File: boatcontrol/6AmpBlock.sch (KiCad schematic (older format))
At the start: 15 parts, among them U7901 ULN2803A

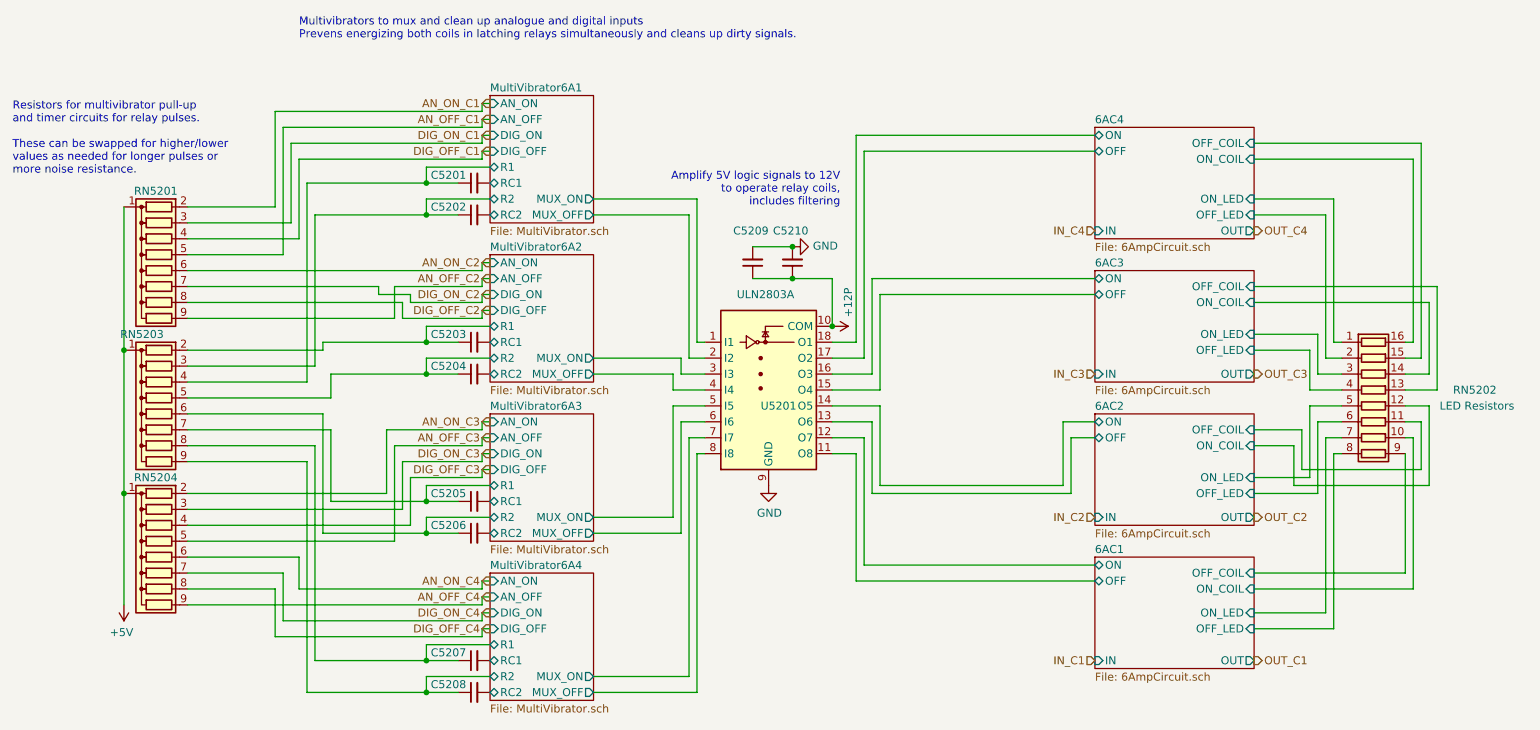
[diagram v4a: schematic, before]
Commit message: Add Node-RED flows
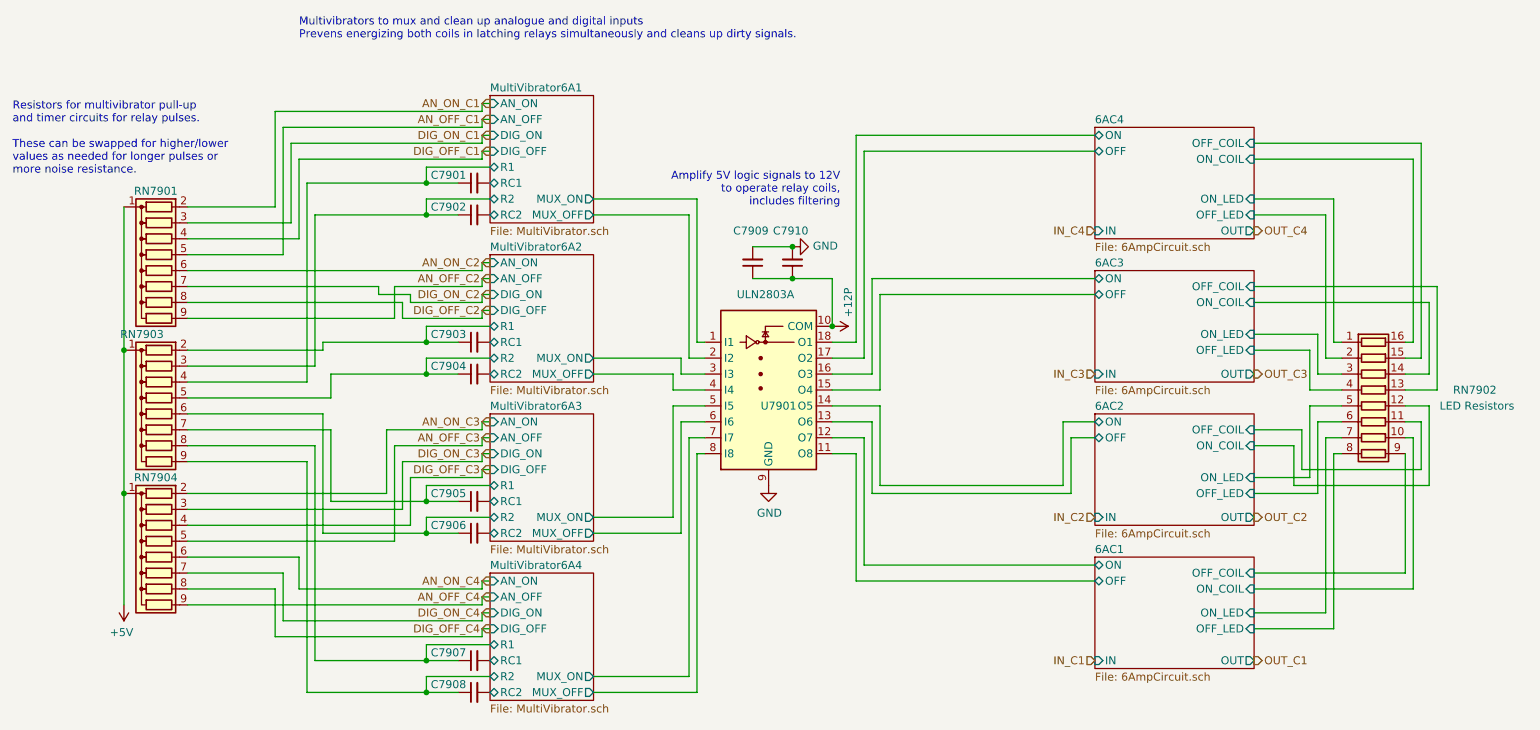
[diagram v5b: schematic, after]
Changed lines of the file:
@@
 $Descr A4 11693 8268
 encoding utf-8
-Sheet 62 97
+Sheet 89 97
 Title "Boat Control Hat"
 Date "2020-07-09"
@@
 AR Path="/D1BB8DB4/5F317CB5/60365AF1" Ref="U7901"  Part="1"
 AR Path="/D1BB8DB4/5F746103/60365AF1" Ref="U5201"  Part="1"
-F 0 "U5201" H 6250 3650 50  0000 L CNN
+F 0 "U7901" H 6250 3650 50  0000 L CNN
 F 1 "ULN2803A" H 6100 4350 50  0000 L CNN
 F 2 "Package_DIP:DIP-18_W7.62mm" H 6350 3200 50  0001 L CNN
@@
 AR Path="/D1BB8DB4/5F317CB5/60365C68" Ref="RN7902"  Part="1"
 AR Path="/D1BB8DB4/5F746103/60365C68" Ref="RN5202"  Part="1"
-F 0 "RN5202" V 10000 4550 50  0000 L CNN
+F 0 "RN7902" V 10000 4550 50  0000 L CNN
 F 1 "680Ω" V 9600 3900 50  0001 L CNN
 F 2 "BoatControl:DIP254P762X432-16P" V 10575 4050 50  0001 C CNN
@@
 AR Path="/D1BB8DB4/5F746103/62AB509B" Ref="C5201"  Part="1"
 AR Path="/D1BB8DB4/5F317CB5/62AB509B" Ref="C7901"  Part="1"
-F 0 "C5201" V 4400 2700 50  0000 L CNN
+F 0 "C7901" V 4400 2700 50  0000 L CNN
 F 1 "1µF" H 3600 2550 50  0001 L CNN
 F 2 "Capacitor_THT:C_Disc_D7.5mm_W5.0mm_P5.00mm" H 4450 2650 50  0001 C CNN
@@
 AR Path="/D1BB8DB4/5F746103/62AC1E93" Ref="C5202"  Part="1"
 AR Path="/D1BB8DB4/5F317CB5/62AC1E93" Ref="C7902"  Part="1"
-F 0 "C5202" V 4400 2900 50  0000 L CNN
+F 0 "C7902" V 4400 2900 50  0000 L CNN
 F 1 "1µF" H 3600 2750 50  0001 L CNN
 F 2 "Capacitor_THT:C_Disc_D7.5mm_W5.0mm_P5.00mm" H 4450 2850 50  0001 C CNN
@@
 AR Path="/D1BB8DB4/5F746103/62ADD9A6" Ref="C5208"  Part="1"
 AR Path="/D1BB8DB4/5F317CB5/62ADD9A6" Ref="C7908"  Part="1"
-F 0 "C5208" V 4400 5900 50  0000 L CNN
+F 0 "C7908" V 4400 5900 50  0000 L CNN
 F 1 "1µF" H 3600 5750 50  0001 L CNN
 F 2 "Capacitor_THT:C_Disc_D7.5mm_W5.0mm_P5.00mm" H 4450 5850 50  0001 C CNN
@@
 AR Path="/D1BB8DB4/5F746103/62AEACF8" Ref="C5207"  Part="1"
 AR Path="/D1BB8DB4/5F317CB5/62AEACF8" Ref="C7907"  Part="1"
-F 0 "C5207" V 4400 5700 50  0000 L CNN
+F 0 "C7907" V 4400 5700 50  0000 L CNN
 F 1 "1µF" H 3600 5550 50  0001 L CNN
 F 2 "Capacitor_THT:C_Disc_D7.5mm_W5.0mm_P5.00mm" H 4450 5650 50  0001 C CNN
@@
 AR Path="/D1BB8DB4/5F746103/62AF81A3" Ref="C5206"  Part="1"
 AR Path="/D1BB8DB4/5F317CB5/62AF81A3" Ref="C7906"  Part="1"
-F 0 "C5206" V 4400 4900 50  0000 L CNN
+F 0 "C7906" V 4400 4900 50  0000 L CNN
 F 1 "1µF" H 3600 4750 50  0001 L CNN
 F 2 "Capacitor_THT:C_Disc_D7.5mm_W5.0mm_P5.00mm" H 4450 4850 50  0001 C CNN
@@
 AR Path="/D1BB8DB4/5F746103/62B05762" Ref="C5205"  Part="1"
 AR Path="/D1BB8DB4/5F317CB5/62B05762" Ref="C7905"  Part="1"
-F 0 "C5205" V 4400 4700 50  0000 L CNN
+F 0 "C7905" V 4400 4700 50  0000 L CNN
 F 1 "1µF" H 3600 4550 50  0001 L CNN
 F 2 "Capacitor_THT:C_Disc_D7.5mm_W5.0mm_P5.00mm" H 4450 4650 50  0001 C CNN
@@
 AR Path="/D1BB8DB4/5F746103/62B3C5BA" Ref="C5203"  Part="1"
 AR Path="/D1BB8DB4/5F317CB5/62B3C5BA" Ref="C7903"  Part="1"
-F 0 "C5203" V 4400 3700 50  0000 L CNN
+F 0 "C7903" V 4400 3700 50  0000 L CNN
 F 1 "1µF" H 3600 3550 50  0001 L CNN
 F 2 "Capacitor_THT:C_Disc_D7.5mm_W5.0mm_P5.00mm" H 4450 3650 50  0001 C CNN
@@
 AR Path="/D1BB8DB4/5F746103/62B4996D" Ref="C5204"  Part="1"
 AR Path="/D1BB8DB4/5F317CB5/62B4996D" Ref="C7904"  Part="1"
-F 0 "C5204" V 4400 3900 50  0000 L CNN
+F 0 "C7904" V 4400 3900 50  0000 L CNN
 F 1 "1µF" H 3600 3750 50  0001 L CNN
 F 2 "Capacitor_THT:C_Disc_D7.5mm_W5.0mm_P5.00mm" H 4450 3850 50  0001 C CNN
@@
 AR Path="/D1BB8DB4/5F317CB5/62C7A7CE" Ref="RN7903"  Part="1"
 AR Path="/D1BB8DB4/5F746103/62C7A7CE" Ref="RN5203"  Part="1"
-F 0 "RN5203" V 1950 4050 50  0000 L CNN
+F 0 "RN7903" V 1950 4050 50  0000 L CNN
 F 1 "10MΩ" H 2100 3700 50  0001 L CNN
 F 2 "Resistor_THT:R_Array_SIP9" V 2925 4100 50  0001 C CNN
@@
 AR Path="/D1BB8DB4/5F317CB5/62F1D24C" Ref="RN7904"  Part="1"
 AR Path="/D1BB8DB4/5F746103/62F1D24C" Ref="RN5204"  Part="1"
-F 0 "RN5204" V 1950 5000 50  0000 C CNN
+F 0 "RN7904" V 1950 5000 50  0000 C CNN
 F 1 "100KΩ" V 2250 4700 50  0001 C CNN
 F 2 "Resistor_THT:R_Array_SIP9" H 3200 5100 50  0001 L CNN
@@
 AR Path="/D1BB8DB4/5F317CB5/62F2A731" Ref="RN7901"  Part="1"
 AR Path="/D1BB8DB4/5F746103/62F2A731" Ref="RN5201"  Part="1"
-F 0 "RN5201" V 1950 3200 50  0000 C CNN
+F 0 "RN7901" V 1950 3200 50  0000 C CNN
 F 1 "100KΩ" V 2250 2900 50  0001 C CNN
 F 2 "Resistor_THT:R_Array_SIP9" H 3200 3300 50  0001 L CNN
@@
 AR Path="/D1BB8DB4/5F317CB5/624D8B2F" Ref="C7909"  Part="1"
 AR Path="/D1BB8DB4/5F746103/624D8B2F" Ref="C5209"  Part="1"
-F 0 "C5209" H 6100 2950 50  0000 L CNN
+F 0 "C7909" H 6100 2950 50  0000 L CNN
 F 1 "10uF" H 6291 3105 50  0001 L CNN
 F 2 "Capacitor_THT:C_Disc_D7.5mm_W5.0mm_P5.00mm" H 6200 3150 50  0001 C CNN
@@
 AR Path="/D1BB8DB4/5F317CB5/624D8B37" Ref="C7910"  Part="1"
 AR Path="/D1BB8DB4/5F746103/624D8B37" Ref="C5210"  Part="1"
-F 0 "C5210" H 6350 2950 50  0000 L CNN
+F 0 "C7910" H 6350 2950 50  0000 L CNN
 F 1 "0.1uF" H 6541 3105 50  0001 L CNN
 F 2 "Capacitor_THT:C_Disc_D7.5mm_W5.0mm_P5.00mm" H 6450 3150 50  0001 C CNN

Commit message: Fix SB footprint and symbol
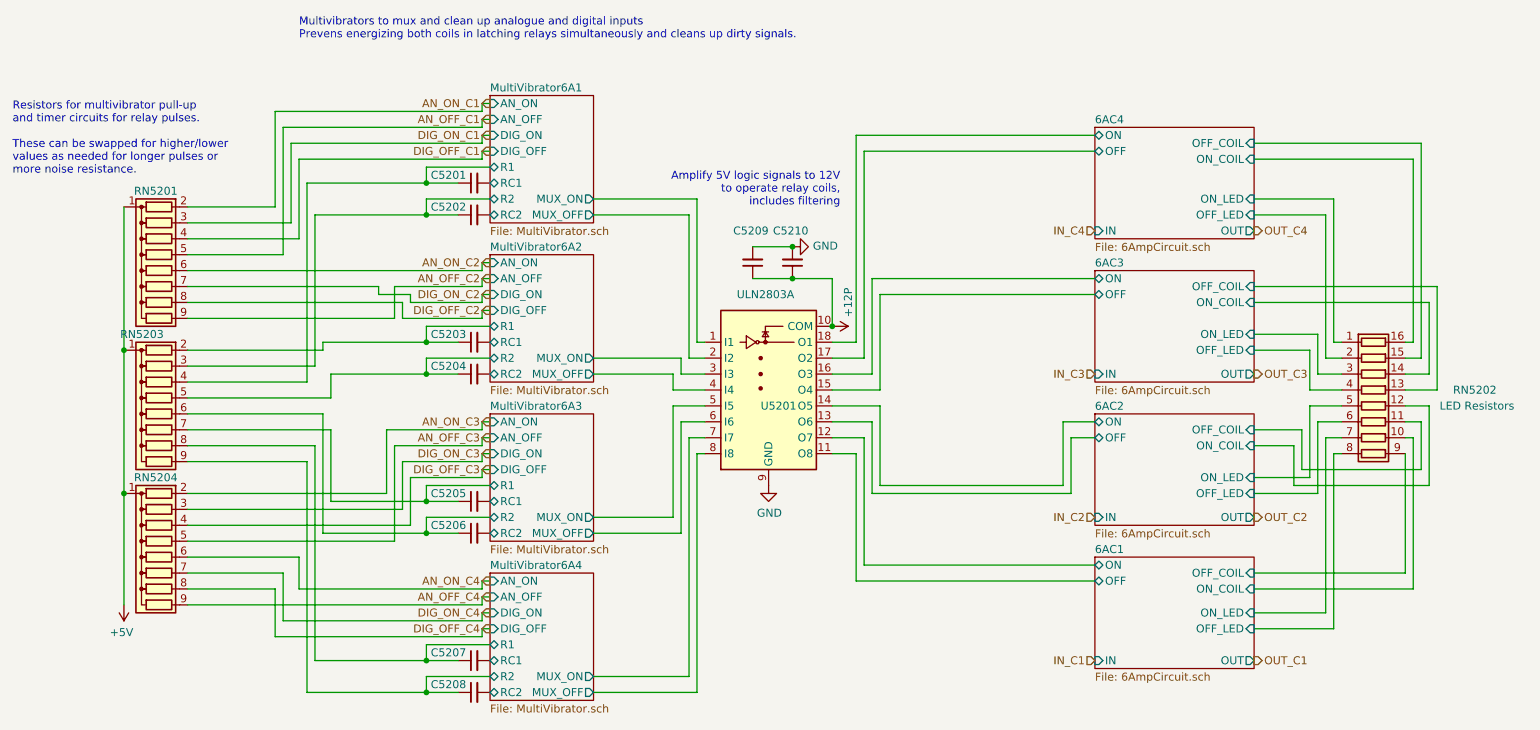
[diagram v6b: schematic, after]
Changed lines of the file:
@@
 $Descr A4 11693 8268
 encoding utf-8
-Sheet 89 97
+Sheet 51 97
 Title "Boat Control Hat"
 Date "2020-07-09"
@@
 AR Path="/D1BB8DB4/5F317CB5/60365AF1" Ref="U7901"  Part="1"
 AR Path="/D1BB8DB4/5F746103/60365AF1" Ref="U5201"  Part="1"
-F 0 "U7901" H 6250 3650 50  0000 L CNN
+F 0 "U5201" H 6250 3650 50  0000 L CNN
 F 1 "ULN2803A" H 6100 4350 50  0000 L CNN
 F 2 "Package_DIP:DIP-18_W7.62mm" H 6350 3200 50  0001 L CNN
@@
 AR Path="/D1BB8DB4/5F317CB5/60365C68" Ref="RN7902"  Part="1"
 AR Path="/D1BB8DB4/5F746103/60365C68" Ref="RN5202"  Part="1"
-F 0 "RN7902" V 10000 4550 50  0000 L CNN
+F 0 "RN5202" V 10000 4550 50  0000 L CNN
 F 1 "680Ω" V 9600 3900 50  0001 L CNN
 F 2 "BoatControl:DIP254P762X432-16P" V 10575 4050 50  0001 C CNN
@@
 AR Path="/D1BB8DB4/5F746103/62AB509B" Ref="C5201"  Part="1"
 AR Path="/D1BB8DB4/5F317CB5/62AB509B" Ref="C7901"  Part="1"
-F 0 "C7901" V 4400 2700 50  0000 L CNN
+F 0 "C5201" V 4400 2700 50  0000 L CNN
 F 1 "1µF" H 3600 2550 50  0001 L CNN
 F 2 "Capacitor_THT:C_Disc_D7.5mm_W5.0mm_P5.00mm" H 4450 2650 50  0001 C CNN
@@
 AR Path="/D1BB8DB4/5F746103/62AC1E93" Ref="C5202"  Part="1"
 AR Path="/D1BB8DB4/5F317CB5/62AC1E93" Ref="C7902"  Part="1"
-F 0 "C7902" V 4400 2900 50  0000 L CNN
+F 0 "C5202" V 4400 2900 50  0000 L CNN
 F 1 "1µF" H 3600 2750 50  0001 L CNN
 F 2 "Capacitor_THT:C_Disc_D7.5mm_W5.0mm_P5.00mm" H 4450 2850 50  0001 C CNN
@@
 AR Path="/D1BB8DB4/5F746103/62ADD9A6" Ref="C5208"  Part="1"
 AR Path="/D1BB8DB4/5F317CB5/62ADD9A6" Ref="C7908"  Part="1"
-F 0 "C7908" V 4400 5900 50  0000 L CNN
+F 0 "C5208" V 4400 5900 50  0000 L CNN
 F 1 "1µF" H 3600 5750 50  0001 L CNN
 F 2 "Capacitor_THT:C_Disc_D7.5mm_W5.0mm_P5.00mm" H 4450 5850 50  0001 C CNN
@@
 AR Path="/D1BB8DB4/5F746103/62AEACF8" Ref="C5207"  Part="1"
 AR Path="/D1BB8DB4/5F317CB5/62AEACF8" Ref="C7907"  Part="1"
-F 0 "C7907" V 4400 5700 50  0000 L CNN
+F 0 "C5207" V 4400 5700 50  0000 L CNN
 F 1 "1µF" H 3600 5550 50  0001 L CNN
 F 2 "Capacitor_THT:C_Disc_D7.5mm_W5.0mm_P5.00mm" H 4450 5650 50  0001 C CNN
@@
 AR Path="/D1BB8DB4/5F746103/62AF81A3" Ref="C5206"  Part="1"
 AR Path="/D1BB8DB4/5F317CB5/62AF81A3" Ref="C7906"  Part="1"
-F 0 "C7906" V 4400 4900 50  0000 L CNN
+F 0 "C5206" V 4400 4900 50  0000 L CNN
 F 1 "1µF" H 3600 4750 50  0001 L CNN
 F 2 "Capacitor_THT:C_Disc_D7.5mm_W5.0mm_P5.00mm" H 4450 4850 50  0001 C CNN
@@
 AR Path="/D1BB8DB4/5F746103/62B05762" Ref="C5205"  Part="1"
 AR Path="/D1BB8DB4/5F317CB5/62B05762" Ref="C7905"  Part="1"
-F 0 "C7905" V 4400 4700 50  0000 L CNN
+F 0 "C5205" V 4400 4700 50  0000 L CNN
 F 1 "1µF" H 3600 4550 50  0001 L CNN
 F 2 "Capacitor_THT:C_Disc_D7.5mm_W5.0mm_P5.00mm" H 4450 4650 50  0001 C CNN
@@
 AR Path="/D1BB8DB4/5F746103/62B3C5BA" Ref="C5203"  Part="1"
 AR Path="/D1BB8DB4/5F317CB5/62B3C5BA" Ref="C7903"  Part="1"
-F 0 "C7903" V 4400 3700 50  0000 L CNN
+F 0 "C5203" V 4400 3700 50  0000 L CNN
 F 1 "1µF" H 3600 3550 50  0001 L CNN
 F 2 "Capacitor_THT:C_Disc_D7.5mm_W5.0mm_P5.00mm" H 4450 3650 50  0001 C CNN
@@
 AR Path="/D1BB8DB4/5F746103/62B4996D" Ref="C5204"  Part="1"
 AR Path="/D1BB8DB4/5F317CB5/62B4996D" Ref="C7904"  Part="1"
-F 0 "C7904" V 4400 3900 50  0000 L CNN
+F 0 "C5204" V 4400 3900 50  0000 L CNN
 F 1 "1µF" H 3600 3750 50  0001 L CNN
 F 2 "Capacitor_THT:C_Disc_D7.5mm_W5.0mm_P5.00mm" H 4450 3850 50  0001 C CNN
@@
 AR Path="/D1BB8DB4/5F317CB5/62C7A7CE" Ref="RN7903"  Part="1"
 AR Path="/D1BB8DB4/5F746103/62C7A7CE" Ref="RN5203"  Part="1"
-F 0 "RN7903" V 1950 4050 50  0000 L CNN
+F 0 "RN5203" V 1950 4050 50  0000 L CNN
 F 1 "10MΩ" H 2100 3700 50  0001 L CNN
 F 2 "Resistor_THT:R_Array_SIP9" V 2925 4100 50  0001 C CNN
@@
 AR Path="/D1BB8DB4/5F317CB5/62F1D24C" Ref="RN7904"  Part="1"
 AR Path="/D1BB8DB4/5F746103/62F1D24C" Ref="RN5204"  Part="1"
-F 0 "RN7904" V 1950 5000 50  0000 C CNN
+F 0 "RN5204" V 1950 5000 50  0000 C CNN
 F 1 "100KΩ" V 2250 4700 50  0001 C CNN
 F 2 "Resistor_THT:R_Array_SIP9" H 3200 5100 50  0001 L CNN
@@
 AR Path="/D1BB8DB4/5F317CB5/62F2A731" Ref="RN7901"  Part="1"
 AR Path="/D1BB8DB4/5F746103/62F2A731" Ref="RN5201"  Part="1"
-F 0 "RN7901" V 1950 3200 50  0000 C CNN
+F 0 "RN5201" V 1950 3200 50  0000 C CNN
 F 1 "100KΩ" V 2250 2900 50  0001 C CNN
 F 2 "Resistor_THT:R_Array_SIP9" H 3200 3300 50  0001 L CNN
@@
 AR Path="/D1BB8DB4/5F317CB5/624D8B2F" Ref="C7909"  Part="1"
 AR Path="/D1BB8DB4/5F746103/624D8B2F" Ref="C5209"  Part="1"
-F 0 "C7909" H 6100 2950 50  0000 L CNN
+F 0 "C5209" H 6100 2950 50  0000 L CNN
 F 1 "10uF" H 6291 3105 50  0001 L CNN
 F 2 "Capacitor_THT:C_Disc_D7.5mm_W5.0mm_P5.00mm" H 6200 3150 50  0001 C CNN
@@
 AR Path="/D1BB8DB4/5F317CB5/624D8B37" Ref="C7910"  Part="1"
 AR Path="/D1BB8DB4/5F746103/624D8B37" Ref="C5210"  Part="1"
-F 0 "C7910" H 6350 2950 50  0000 L CNN
+F 0 "C5210" H 6350 2950 50  0000 L CNN
 F 1 "0.1uF" H 6541 3105 50  0001 L CNN
 F 2 "Capacitor_THT:C_Disc_D7.5mm_W5.0mm_P5.00mm" H 6450 3150 50  0001 C CNN

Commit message: Cleanup
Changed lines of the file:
@@
 AR Path="/D1BB8DB4/5F317CB5/60365AF1" Ref="U7901"  Part="1"
 AR Path="/D1BB8DB4/5F746103/60365AF1" Ref="U5201"  Part="1"
-F 0 "U5201" H 6250 3650 50  0000 L CNN
+F 0 "U7901" H 6250 3650 50  0000 L CNN
 F 1 "ULN2803A" H 6100 4350 50  0000 L CNN
 F 2 "Package_DIP:DIP-18_W7.62mm" H 6350 3200 50  0001 L CNN
@@
 AR Path="/D1BB8DB4/5F317CB5/60365C68" Ref="RN7902"  Part="1"
 AR Path="/D1BB8DB4/5F746103/60365C68" Ref="RN5202"  Part="1"
-F 0 "RN5202" V 10000 4550 50  0000 L CNN
+F 0 "RN7902" V 10000 4550 50  0000 L CNN
 F 1 "680Ω" V 9600 3900 50  0001 L CNN
 F 2 "BoatControl:DIP254P762X432-16P" V 10575 4050 50  0001 C CNN
@@
 AR Path="/D1BB8DB4/5F746103/62AB509B" Ref="C5201"  Part="1"
 AR Path="/D1BB8DB4/5F317CB5/62AB509B" Ref="C7901"  Part="1"
-F 0 "C5201" V 4400 2700 50  0000 L CNN
+F 0 "C7901" V 4400 2700 50  0000 L CNN
 F 1 "1µF" H 3600 2550 50  0001 L CNN
 F 2 "Capacitor_THT:C_Disc_D7.5mm_W5.0mm_P5.00mm" H 4450 2650 50  0001 C CNN
@@
 AR Path="/D1BB8DB4/5F746103/62AC1E93" Ref="C5202"  Part="1"
 AR Path="/D1BB8DB4/5F317CB5/62AC1E93" Ref="C7902"  Part="1"
-F 0 "C5202" V 4400 2900 50  0000 L CNN
+F 0 "C7902" V 4400 2900 50  0000 L CNN
 F 1 "1µF" H 3600 2750 50  0001 L CNN
 F 2 "Capacitor_THT:C_Disc_D7.5mm_W5.0mm_P5.00mm" H 4450 2850 50  0001 C CNN
@@
 AR Path="/D1BB8DB4/5F746103/62ADD9A6" Ref="C5208"  Part="1"
 AR Path="/D1BB8DB4/5F317CB5/62ADD9A6" Ref="C7908"  Part="1"
-F 0 "C5208" V 4400 5900 50  0000 L CNN
+F 0 "C7908" V 4400 5900 50  0000 L CNN
 F 1 "1µF" H 3600 5750 50  0001 L CNN
 F 2 "Capacitor_THT:C_Disc_D7.5mm_W5.0mm_P5.00mm" H 4450 5850 50  0001 C CNN
@@
 AR Path="/D1BB8DB4/5F746103/62AEACF8" Ref="C5207"  Part="1"
 AR Path="/D1BB8DB4/5F317CB5/62AEACF8" Ref="C7907"  Part="1"
-F 0 "C5207" V 4400 5700 50  0000 L CNN
+F 0 "C7907" V 4400 5700 50  0000 L CNN
 F 1 "1µF" H 3600 5550 50  0001 L CNN
 F 2 "Capacitor_THT:C_Disc_D7.5mm_W5.0mm_P5.00mm" H 4450 5650 50  0001 C CNN
@@
 AR Path="/D1BB8DB4/5F746103/62AF81A3" Ref="C5206"  Part="1"
 AR Path="/D1BB8DB4/5F317CB5/62AF81A3" Ref="C7906"  Part="1"
-F 0 "C5206" V 4400 4900 50  0000 L CNN
+F 0 "C7906" V 4400 4900 50  0000 L CNN
 F 1 "1µF" H 3600 4750 50  0001 L CNN
 F 2 "Capacitor_THT:C_Disc_D7.5mm_W5.0mm_P5.00mm" H 4450 4850 50  0001 C CNN
@@
 AR Path="/D1BB8DB4/5F746103/62B05762" Ref="C5205"  Part="1"
 AR Path="/D1BB8DB4/5F317CB5/62B05762" Ref="C7905"  Part="1"
-F 0 "C5205" V 4400 4700 50  0000 L CNN
+F 0 "C7905" V 4400 4700 50  0000 L CNN
 F 1 "1µF" H 3600 4550 50  0001 L CNN
 F 2 "Capacitor_THT:C_Disc_D7.5mm_W5.0mm_P5.00mm" H 4450 4650 50  0001 C CNN
@@
 AR Path="/D1BB8DB4/5F746103/62B3C5BA" Ref="C5203"  Part="1"
 AR Path="/D1BB8DB4/5F317CB5/62B3C5BA" Ref="C7903"  Part="1"
-F 0 "C5203" V 4400 3700 50  0000 L CNN
+F 0 "C7903" V 4400 3700 50  0000 L CNN
 F 1 "1µF" H 3600 3550 50  0001 L CNN
 F 2 "Capacitor_THT:C_Disc_D7.5mm_W5.0mm_P5.00mm" H 4450 3650 50  0001 C CNN
@@
 AR Path="/D1BB8DB4/5F746103/62B4996D" Ref="C5204"  Part="1"
 AR Path="/D1BB8DB4/5F317CB5/62B4996D" Ref="C7904"  Part="1"
-F 0 "C5204" V 4400 3900 50  0000 L CNN
+F 0 "C7904" V 4400 3900 50  0000 L CNN
 F 1 "1µF" H 3600 3750 50  0001 L CNN
 F 2 "Capacitor_THT:C_Disc_D7.5mm_W5.0mm_P5.00mm" H 4450 3850 50  0001 C CNN
@@
 AR Path="/D1BB8DB4/5F317CB5/62C7A7CE" Ref="RN7903"  Part="1"
 AR Path="/D1BB8DB4/5F746103/62C7A7CE" Ref="RN5203"  Part="1"
-F 0 "RN5203" V 1950 4050 50  0000 L CNN
+F 0 "RN7903" V 1950 4050 50  0000 L CNN
 F 1 "10MΩ" H 2100 3700 50  0001 L CNN
 F 2 "Resistor_THT:R_Array_SIP9" V 2925 4100 50  0001 C CNN
@@
 AR Path="/D1BB8DB4/5F317CB5/62F1D24C" Ref="RN7904"  Part="1"
 AR Path="/D1BB8DB4/5F746103/62F1D24C" Ref="RN5204"  Part="1"
-F 0 "RN5204" V 1950 5000 50  0000 C CNN
+F 0 "RN7904" V 1950 5000 50  0000 C CNN
 F 1 "100KΩ" V 2250 4700 50  0001 C CNN
 F 2 "Resistor_THT:R_Array_SIP9" H 3200 5100 50  0001 L CNN
@@
 AR Path="/D1BB8DB4/5F317CB5/62F2A731" Ref="RN7901"  Part="1"
 AR Path="/D1BB8DB4/5F746103/62F2A731" Ref="RN5201"  Part="1"
-F 0 "RN5201" V 1950 3200 50  0000 C CNN
+F 0 "RN7901" V 1950 3200 50  0000 C CNN
 F 1 "100KΩ" V 2250 2900 50  0001 C CNN
 F 2 "Resistor_THT:R_Array_SIP9" H 3200 3300 50  0001 L CNN
@@
 AR Path="/D1BB8DB4/5F317CB5/624D8B2F" Ref="C7909"  Part="1"
 AR Path="/D1BB8DB4/5F746103/624D8B2F" Ref="C5209"  Part="1"
-F 0 "C5209" H 6100 2950 50  0000 L CNN
+F 0 "C7909" H 6100 2950 50  0000 L CNN
 F 1 "10uF" H 6291 3105 50  0001 L CNN
 F 2 "Capacitor_THT:C_Disc_D7.5mm_W5.0mm_P5.00mm" H 6200 3150 50  0001 C CNN
@@
 AR Path="/D1BB8DB4/5F317CB5/624D8B37" Ref="C7910"  Part="1"
 AR Path="/D1BB8DB4/5F746103/624D8B37" Ref="C5210"  Part="1"
-F 0 "C5210" H 6350 2950 50  0000 L CNN
+F 0 "C7910" H 6350 2950 50  0000 L CNN
 F 1 "0.1uF" H 6541 3105 50  0001 L CNN
 F 2 "Capacitor_THT:C_Disc_D7.5mm_W5.0mm_P5.00mm" H 6450 3150 50  0001 C CNN
